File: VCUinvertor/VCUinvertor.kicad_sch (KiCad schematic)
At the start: 119 parts, among them J7 PowerSupply, J9 BRAKE LIGHT, Q1 2N7002, Q10 2N7002, Q11 BC848C, Q12 BCP51, Q2 2N7002, Q3 2N7002, Q4 2N7002, Q5 2N7002, Q6 2N7002, Q7 2N7002, Q8 2N7002, Q9 2N7002, U1 TJA1448ATK, U2 REF3433T, U3 TLV76150DCY

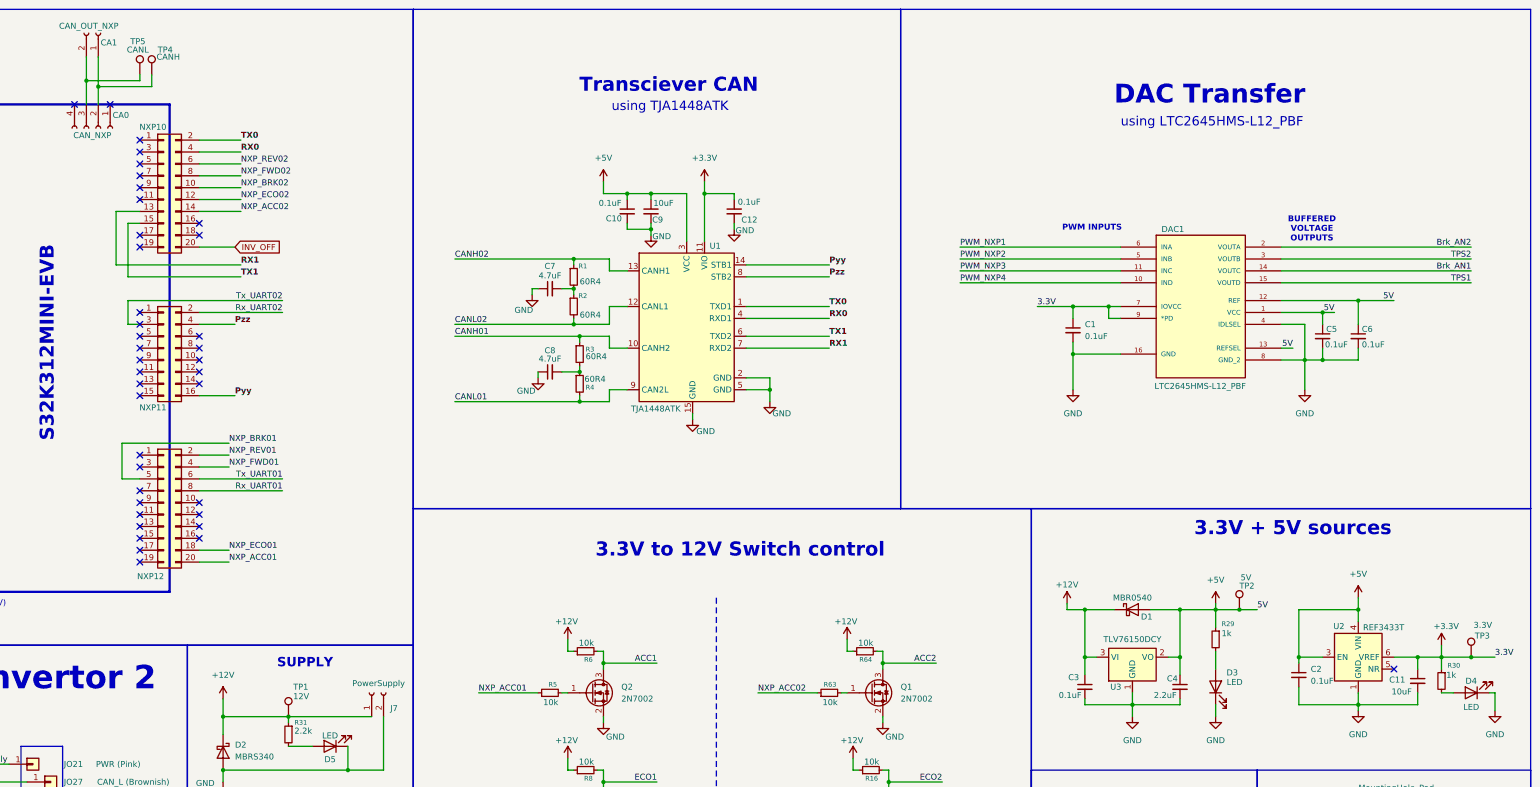
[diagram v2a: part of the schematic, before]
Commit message: Ref LEDs added
For 3.3V & 5V & ...
Added for easy testing, LEDs running 2-3 mA each
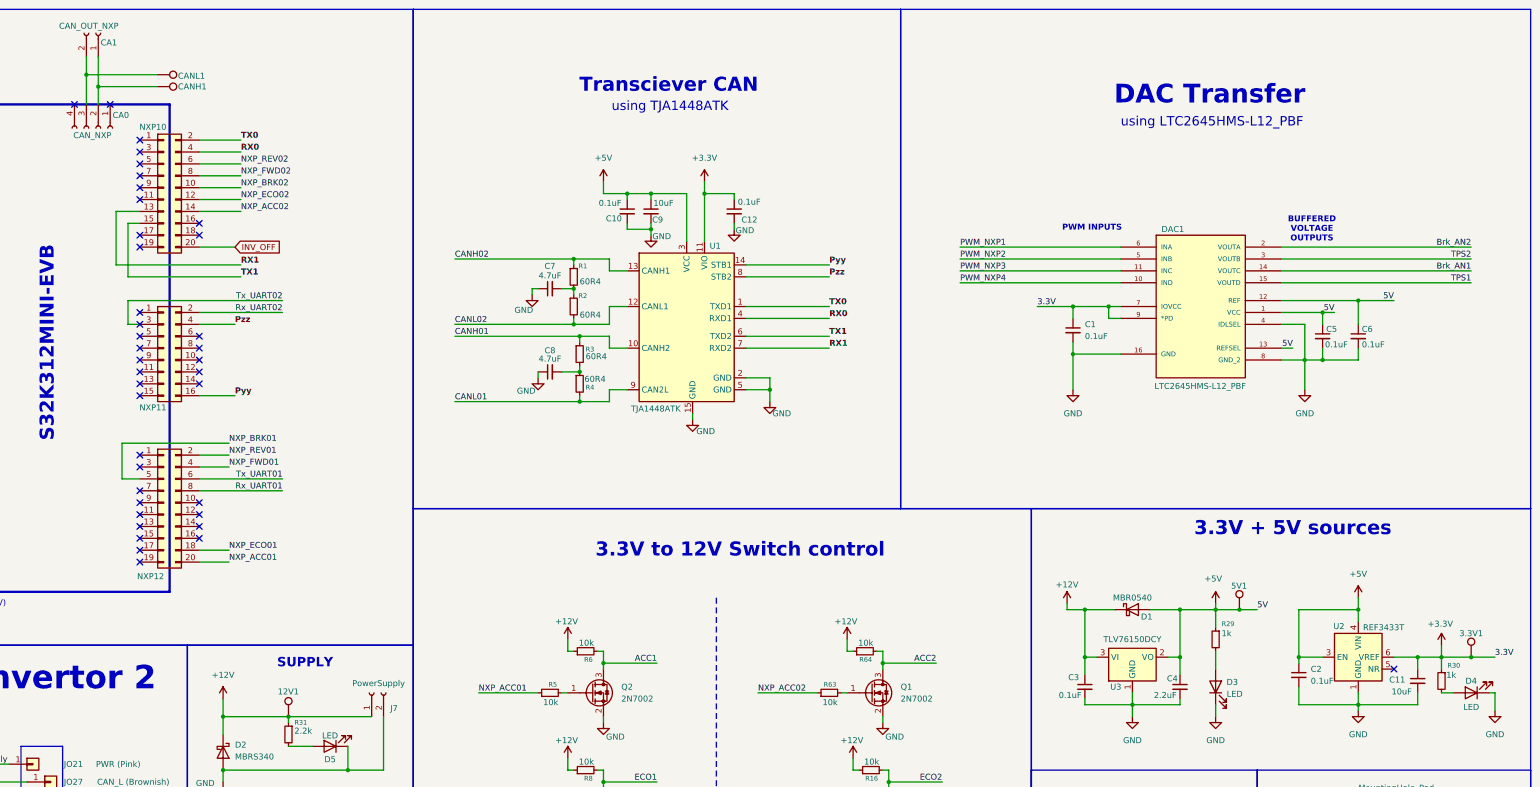
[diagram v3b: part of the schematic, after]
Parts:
- renumbered TP1 to 12V1, TP3 to 3.3V1, TP2 to 5V1, TP4 to CANH1, TP5 to CANL1
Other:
- moved on the sheet: CANH1, CANL1
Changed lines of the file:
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@@
 	)
 	(junction
+		(at 97.79 26.67)
+		(diameter 0)
+		(color 0 0 0 0)
+	)
+	(junction
 		(at 69.85 227.33)
 		(diameter 0)
@@
 	)
 	(junction
-		(at 97.79 27.94)
-		(diameter 0)
-		(color 0 0 0 0)
-	)
-	(junction
 		(at 361.95 77.47)
 		(diameter 0)
@@
 	(wire
 		(pts
-			(xy 111.76 26.67) (xy 111.76 29.21)
-		)
-		(stroke
-			(width 0)
-			(type default)
-		)
-	)
-	(wire
-		(pts
 			(xy 121.92 45.72) (xy 130.81 45.72)
 		)
@@
 	(wire
 		(pts
-			(xy 97.79 22.86) (xy 97.79 27.94)
+			(xy 97.79 22.86) (xy 97.79 26.67)
 		)
 		(stroke
@@
 	(wire
 		(pts
-			(xy 109.22 27.94) (xy 109.22 26.67)
-		)
-		(stroke
-			(width 0)
-			(type default)
-		)
-	)
-	(wire
-		(pts
 			(xy 100.33 29.21) (xy 100.33 33.02)
 		)
@@
 	(wire
 		(pts
-			(xy 97.79 27.94) (xy 109.22 27.94)
+			(xy 97.79 26.67) (xy 113.03 26.67)
 		)
 		(stroke
@@
 	(wire
 		(pts
+			(xy 97.79 26.67) (xy 97.79 33.02)
+		)
+		(stroke
+			(width 0)
+			(type default)
+		)
+	)
+	(wire
+		(pts
 			(xy 71.12 30.48) (xy 71.12 43.18)
 		)
@@
 	(wire
 		(pts
-			(xy 111.76 29.21) (xy 100.33 29.21)
+			(xy 113.03 29.21) (xy 100.33 29.21)
 		)
 		(stroke
@@
 	(wire
 		(pts
-			(xy 97.79 27.94) (xy 97.79 33.02)
-		)
-		(stroke
-			(width 0)
-			(type default)
-		)
-	)
-	(wire
-		(pts
 			(xy 388.62 237.49) (xy 388.62 241.3)
 		)
@@
 		(on_board yes)
 		(dnp no)
-		(property "Reference" "TP3"
-			(at 394.462 146.558 0)
+		(property "Reference" "3.3V1"
+			(at 391.16 146.05 0)
 			(effects
 				(font
@@
 				)
 				(justify left)
+				(hide yes)
 			)
 		)
@@
 			(project "VCUinvertor"
 				(path "/2b4b6758-f217-4dbc-8f9c-9ada5d4e488c"
-					(reference "TP3")
+					(reference "3.3V1")
 					(unit 1)
 				)
@@
 		(dnp no)
 		(property "Reference" "D3"
-			(at 342.646 154.432 90)
+			(at 342.646 156.464 90)
 			(effects
 				(font
@@
 		)
 		(property "Value" "LED"
-			(at 343.154 156.464 90)
+			(at 343.154 159.004 90)
 			(effects
 				(font
@@
 		(on_board yes)
 		(dnp no)
-		(property "Reference" "TP2"
-			(at 344.17 135.89 0)
+		(property "Reference" "5V1"
+			(at 342.392 135.89 0)
 			(effects
 				(font
@@
 				)
 				(justify left)
+				(hide yes)
 			)
 		)
@@
 			(project "VCUinvertor"
 				(path "/2b4b6758-f217-4dbc-8f9c-9ada5d4e488c"
-					(reference "TP2")
+					(reference "5V1")
 					(unit 1)
 				)
@@
 	(symbol
 		(lib_id "Connector:TestPoint")
-		(at 111.76 26.67 0)
+		(at 113.03 29.21 270)
 		(unit 1)
 		(exclude_from_sim no)
@@
 		(on_board yes)
 		(dnp no)
-		(property "Reference" "TP4"
-			(at 113.03 21.336 0)
+		(property "Reference" "CANH1"
+			(at 117.348 29.21 90)
 			(effects
 				(font
@@
 		)
 		(property "Value" "CANH"
-			(at 112.776 22.86 0)
+			(at 116.84 30.226 0)
 			(effects
 				(font
@@
 				)
 				(justify left)
+				(hide yes)
 			)
 		)
 		(property "Footprint" "TestPoint:TestPoint_Pad_D1.5mm"
-			(at 116.84 26.67 0)
+			(at 113.03 34.29 0)
 			(effects
 				(font
@@
 		)
 		(property "Datasheet" "~"
-			(at 116.84 26.67 0)
+			(at 113.03 34.29 0)
 			(effects
 				(font
@@
 		)
 		(property "Description" "test point"
-			(at 111.76 26.67 0)
+			(at 113.03 29.21 0)
 			(effects
 				(font
@@
 			(project "VCUinvertor"
 				(path "/2b4b6758-f217-4dbc-8f9c-9ada5d4e488c"
-					(reference "TP4")
+					(reference "CANH1")
 					(unit 1)
 				)
@@
 		(on_board yes)
 		(dnp no)
-		(fields_autoplaced yes)
 		(property "Reference" "#PWR052"
 			(at 339.09 143.51 0)
@@
 		)
 		(property "Value" "+5V"
-			(at 339.09 134.62 0)
+			(at 338.582 134.366 0)
 			(effects
 				(font
@@
 	(symbol
 		(lib_id "Connector:TestPoint")
-		(at 109.22 26.67 0)
+		(at 113.03 26.67 270)
 		(unit 1)
 		(exclude_from_sim no)
@@
 		(on_board yes)
 		(dnp no)
-		(property "Reference" "TP5"
-			(at 107.188 19.558 0)
+		(property "Reference" "CANL1"
+			(at 117.348 26.924 90)
 			(effects
 				(font
@@
 		)
 		(property "Value" "CANL"
-			(at 106.426 21.336 0)
+			(at 118.364 23.876 0)
 			(effects
 				(font
@@
 				)
 				(justify left)
+				(hide yes)
 			)
 		)
 		(property "Footprint" "TestPoint:TestPoint_Pad_D1.5mm"
-			(at 114.3 26.67 0)
+			(at 113.03 31.75 0)
 			(effects
 				(font
@@
 		)
 		(property "Datasheet" "~"
-			(at 114.3 26.67 0)
+			(at 113.03 31.75 0)
 			(effects
 				(font
@@
 		)
 		(property "Description" "test point"
-			(at 109.22 26.67 0)
+			(at 113.03 26.67 0)
 			(effects
 				(font
@@
 			(project "VCUinvertor"
 				(path "/2b4b6758-f217-4dbc-8f9c-9ada5d4e488c"
-					(reference "TP5")
+					(reference "CANL1")
 					(unit 1)
 				)
@@
 		)
 		(property "Value" "+3.3V"
-			(at 388.366 144.526 0)
+			(at 387.096 144.018 0)
 			(effects
 				(font
@@
 		(on_board yes)
 		(dnp no)
-		(property "Reference" "TP1"
-			(at 141.986 157.48 0)
+		(property "Reference" "12V1"
+			(at 138.684 158.496 0)
 			(effects
 				(font
@@
 				)
 				(justify left)
+				(hide yes)
 			)
 		)
@@
 			(project ""
 				(path "/2b4b6758-f217-4dbc-8f9c-9ada5d4e488c"
-					(reference "TP1")
+					(reference "12V1")
 					(unit 1)
 				)
